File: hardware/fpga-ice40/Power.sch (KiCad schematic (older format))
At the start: 11 parts, among them J1 Conn_01x03, U2 AZ1117-3.3, U3 AZ1117-1.2

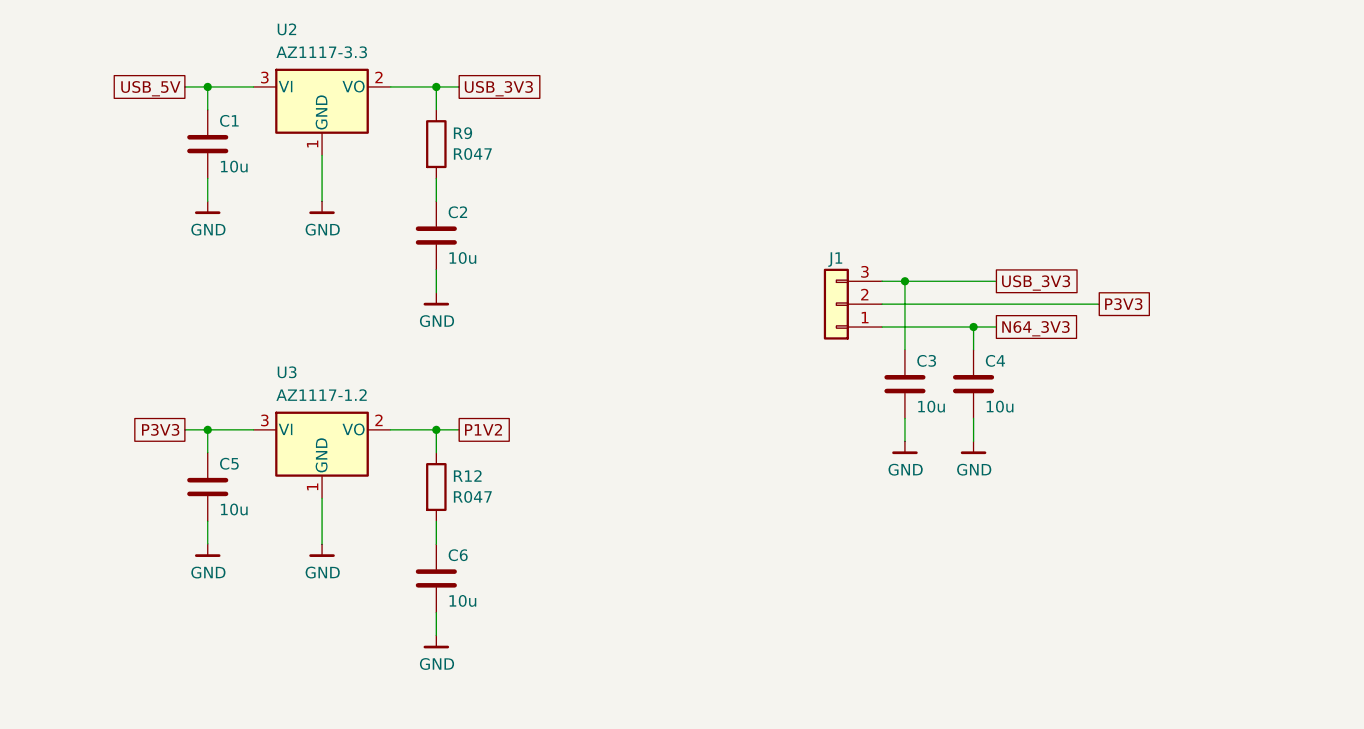
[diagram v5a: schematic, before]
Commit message: Clean up configuration and flash memory routing
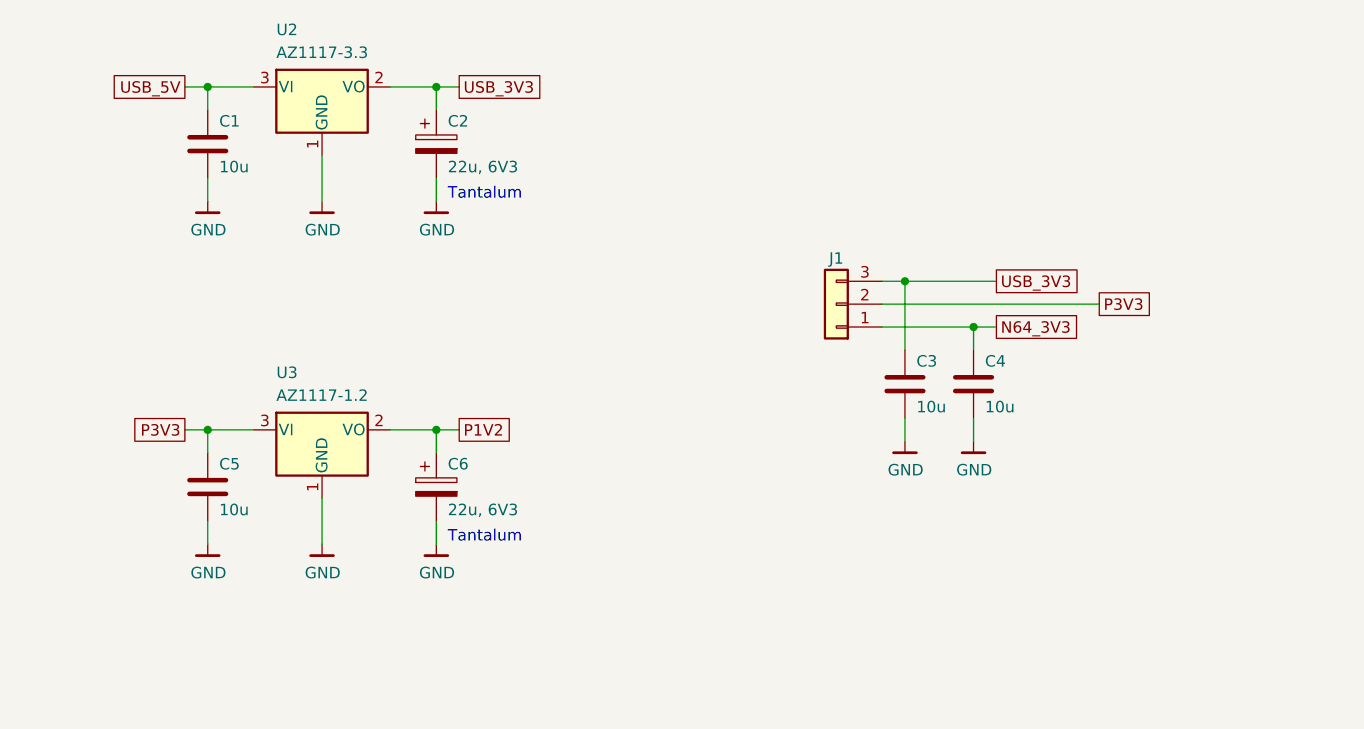
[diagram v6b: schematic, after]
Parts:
- removed C2, C6: 10u, Capacitor_SMD:C_0805_2012Metric, symbol Device:C
- removed R12, R9: R047, Resistor_SMD:R_0603_1608Metric, symbol Device:R
- added C2, C6: 22u, 6V3, Capacitor_Tantalum_SMD:CP_EIA-2012-15_AVX-P, symbol Device:CP
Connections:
- net GND: now also C2.2, C6.2
- net P1V2: now also C6.1
- net USB_3V3: now also C2.1
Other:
- note added: "Tantalum"
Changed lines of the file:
@@
-	1    0    0    -1
-$EndComp
-$Comp
-L Device:C C?
-U 1 1 5F820EC4
-P 4450 3650
-AR Path="/5F820EC4" Ref="C?"  Part="1"
-AR Path="/5F7F68FE/5F820EC4" Ref="C2"  Part="1"
-F 0 "C2" H 4500 3750 50  0000 L CNN
-F 1 "10u" H 4500 3550 50  0000 L CNN
-F 2 "Capacitor_SMD:C_0805_2012Metric" H 4488 3500 50  0001 C CNN
-F 3 "~" H 4450 3650 50  0001 C CNN
-F 4 "CL21A106KAYNNNE" H 4450 3650 50  0001 C CNN "MPN"
-	1    4450 3650
 	1    0    0    -1
 $EndComp
@@
 Wire Wire Line
 	3450 3000 3650 3000
-Wire Wire Line
-	4450 3500 4450 3400
 Wire Wire Line
 	3450 3400 3450 3500
@@
 $EndComp
 Wire Wire Line
-	4450 3800 4450 3900
+	4450 3400 4450 3500
 $Comp
 L ng_power:GND #PWR?
 U 1 1 5F820ED9
-P 4450 3900
+P 4450 3500
 AR Path="/5F820ED9" Ref="#PWR?"  Part="1"
 AR Path="/5F7F68FE/5F820ED9" Ref="#PWR03"  Part="1"
-F 0 "#PWR03" H 4450 3650 50  0001 C CNN
-F 1 "GND" H 4453 3774 50  0000 C CNN
-F 2 "" H 4350 3550 50  0001 C CNN
-F 3 "" H 4450 3900 50  0001 C CNN
-	1    4450 3900
+F 0 "#PWR03" H 4450 3250 50  0001 C CNN
+F 1 "GND" H 4453 3374 50  0000 C CNN
+F 2 "" H 4350 3150 50  0001 C CNN
+F 3 "" H 4450 3500 50  0001 C CNN
+	1    4450 3500
 	1    0    0    -1
 $EndComp
@@
 	1    0    0    -1
 $EndComp
-$Comp
-L Device:C C?
-U 1 1 5F820EF4
-P 4450 5150
-AR Path="/5F820EF4" Ref="C?"  Part="1"
-AR Path="/5F7F68FE/5F820EF4" Ref="C6"  Part="1"
-F 0 "C6" H 4500 5250 50  0000 L CNN
-F 1 "10u" H 4500 5050 50  0000 L CNN
-F 2 "Capacitor_SMD:C_0805_2012Metric" H 4488 5000 50  0001 C CNN
-F 3 "~" H 4450 5150 50  0001 C CNN
-F 4 "CL21A106KAYNNNE" H 4450 5150 50  0001 C CNN "MPN"
-	1    4450 5150
-	1    0    0    -1
-$EndComp
 Wire Wire Line
 	3450 4600 3450 4500
@@
 Wire Wire Line
 	3450 4500 3650 4500
-Wire Wire Line
-	4450 5000 4450 4900
 Wire Wire Line
 	3450 4900 3450 5000
@@
 F 3 "" H 3450 5000 50  0001 C CNN
 	1    3450 5000
-	1    0    0    -1
-$EndComp
-Wire Wire Line
-	4450 5300 4450 5400
-$Comp
-L ng_power:GND #PWR?
-U 1 1 5F820F09
-P 4450 5400
-AR Path="/5F820F09" Ref="#PWR?"  Part="1"
-AR Path="/5F7F68FE/5F820F09" Ref="#PWR08"  Part="1"
-F 0 "#PWR08" H 4450 5150 50  0001 C CNN
-F 1 "GND" H 4453 5274 50  0000 C CNN
-F 2 "" H 4350 5050 50  0001 C CNN
-F 3 "" H 4450 5400 50  0001 C CNN
-	1    4450 5400
 	1    0    0    -1
 $EndComp
@@
 Wire Wire Line
 	4250 3000 4450 3000
-$Comp
-L Device:R R9
-U 1 1 5EFC737A
-P 4450 3250
-F 0 "R9" H 4520 3296 50  0000 L CNN
-F 1 "R047" H 4520 3205 50  0000 L CNN
-F 2 "Resistor_SMD:R_0603_1608Metric" V 4380 3250 50  0001 C CNN
-F 3 "~" H 4450 3250 50  0001 C CNN
-	1    4450 3250
-	1    0    0    -1
-$EndComp
 Wire Wire Line
 	4450 3100 4450 3000
@@
 Wire Wire Line
 	4250 4500 4450 4500
-$Comp
-L Device:R R12
-U 1 1 5EFCE0BE
-P 4450 4750
-F 0 "R12" H 4520 4796 50  0000 L CNN
-F 1 "R047" H 4520 4705 50  0000 L CNN
-F 2 "Resistor_SMD:R_0603_1608Metric" V 4380 4750 50  0001 C CNN
-F 3 "~" H 4450 4750 50  0001 C CNN
-	1    4450 4750
-	1    0    0    -1
-$EndComp
 Wire Wire Line
 	4450 4600 4450 4500
@@
 Wire Wire Line
 	4450 4500 4550 4500
+$Comp
+L Device:CP C2
+U 1 1 5F44244C
+P 4450 3250
+F 0 "C2" H 4500 3350 50  0000 L CNN
+F 1 "22u, 6V3" H 4500 3150 50  0000 L CNN
+F 2 "Capacitor_Tantalum_SMD:CP_EIA-2012-15_AVX-P" H 4488 3100 50  0001 C CNN
+F 3 "~" H 4450 3250 50  0001 C CNN
+F 4 "TAJP226M006RNJ" H 4450 3250 50  0001 C CNN "MPN"
+	1    4450 3250
+	1    0    0    -1
+$EndComp
+Text Notes 4500 3500 0    50   ~ 0
+Tantalum
+Wire Wire Line
+	4450 4900 4450 5000
+$Comp
+L ng_power:GND #PWR?
+U 1 1 5F444790
+P 4450 5000
+AR Path="/5F444790" Ref="#PWR?"  Part="1"
+AR Path="/5F7F68FE/5F444790" Ref="#PWR08"  Part="1"
+F 0 "#PWR08" H 4450 4750 50  0001 C CNN
+F 1 "GND" H 4453 4874 50  0000 C CNN
+F 2 "" H 4350 4650 50  0001 C CNN
+F 3 "" H 4450 5000 50  0001 C CNN
+	1    4450 5000
+	1    0    0    -1
+$EndComp
+$Comp
+L Device:CP C6
+U 1 1 5F44479B
+P 4450 4750
+F 0 "C6" H 4500 4850 50  0000 L CNN
+F 1 "22u, 6V3" H 4500 4650 50  0000 L CNN
+F 2 "Capacitor_Tantalum_SMD:CP_EIA-2012-15_AVX-P" H 4488 4600 50  0001 C CNN
+F 3 "~" H 4450 4750 50  0001 C CNN
+F 4 "TAJP226M006RNJ" H 4450 4750 50  0001 C CNN "MPN"
+	1    4450 4750
+	1    0    0    -1
+$EndComp
+Text Notes 4500 5000 0    50   ~ 0
+Tantalum
 $EndSCHEMATC

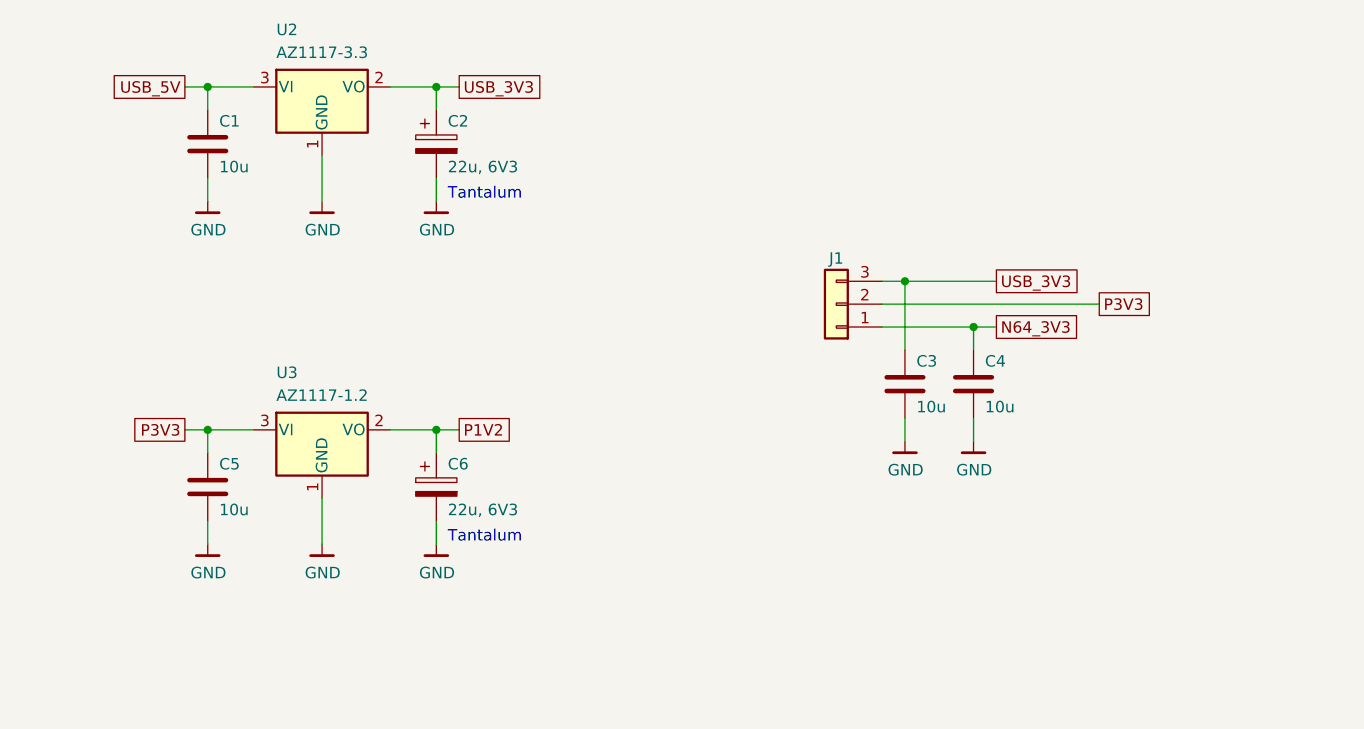
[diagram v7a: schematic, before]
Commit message: Beginning layout of power muxing module
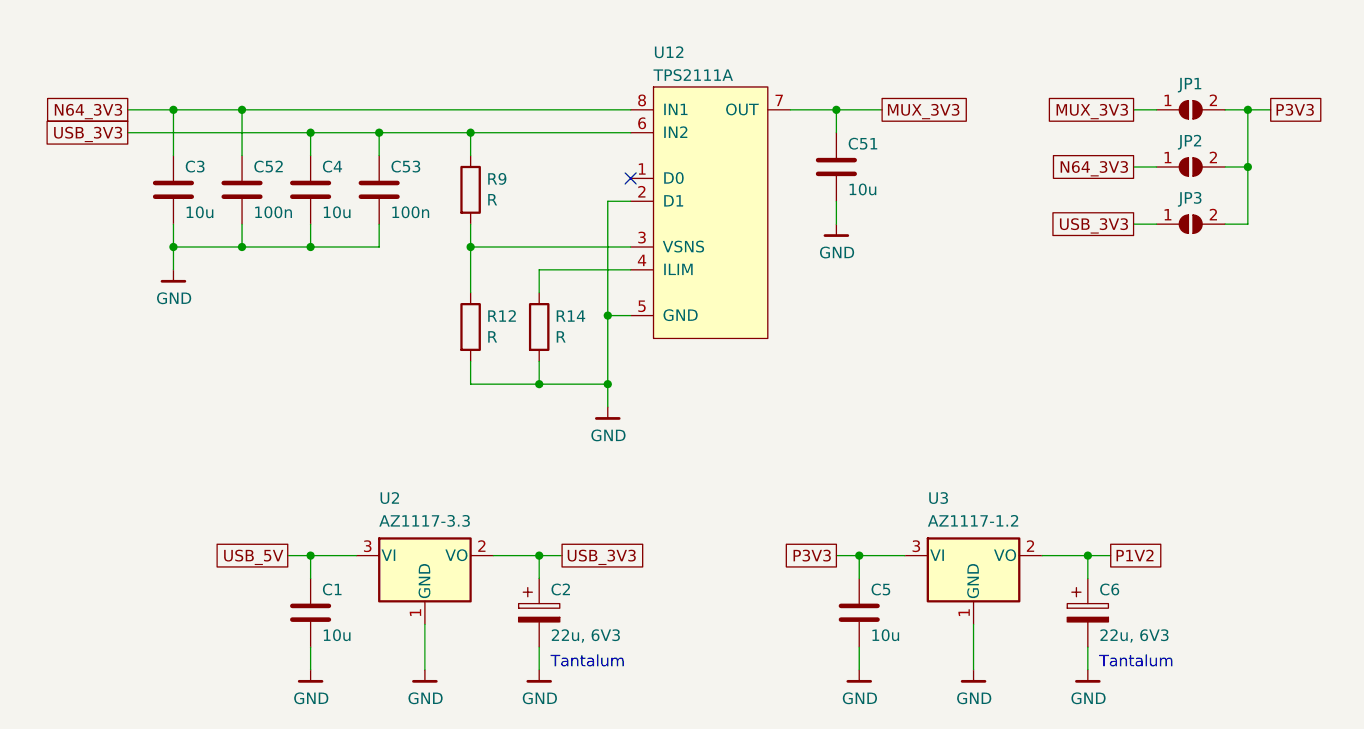
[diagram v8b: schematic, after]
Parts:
- removed J1: Conn_01x03, Connector_PinHeader_2.54mm:PinHeader_1x03_P2.54mm_Vertical, symbol Connector_Generic:Conn_01x03
- added C51: 10u, Capacitor_SMD:C_0805_2012Metric, symbol Device:C
- added C52, C53: 100n, Capacitor_SMD:C_0603_1608Metric, symbol Device:C
- added JP1, JP2, JP3: SolderJumper_2_Open, Jumper:SolderJumper-2_P1.3mm_Open_TrianglePad1.0x1.5mm, symbol Jumper:SolderJumper_2_Open
- added R12, R14, R9: R, Resistor_SMD:R_0603_1608Metric, symbol Device:R
- added U12: TPS2111A, Package_SO:TSSOP-8_4.4x3mm_P0.65mm, symbol ng_pmic:TPS2111A
- C3, C4: MPN CL21A106KAYNNNE -> (none)
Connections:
- net GND: now also C51.2, C52.2, C53.2, R12.2, R14.2, U12.2 (D1), U12.5 (GND)
- net N64_3V3: now also C3.1, C52.1, JP2.1 (A), U12.8 (IN1); no longer C4.1
- net P3V3: now also JP1.2 (B), JP2.2 (B), JP3.2 (B)
- net USB_3V3: now also C4.1, C53.1, JP3.1 (A), R9.1, U12.6 (IN2); no longer C3.1
- new net: R12.1, R9.2, U12.3 (VSNS)
- new net: R14.1, U12.4 (ILIM)
- new net MUX_3V3: C51.1, JP1.1 (A), U12.7 (OUT)
- no-connect marks 0 -> 1
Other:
- moved on the sheet: C1, C2, C3, C4, C5, C6, U2, U3
